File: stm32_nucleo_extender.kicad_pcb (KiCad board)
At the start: 2 copper layers, 103.8 x 162.9 mm, 6 parts, among them CN10 6-534206-9, CN7 6-534206-9, J1 TBL009-254-20GY-2GY, J2 TBL009-254-20GY-2GY, J3 TBL009-254-20GY-2GY, J4 TBL009-254-20GY-2GY

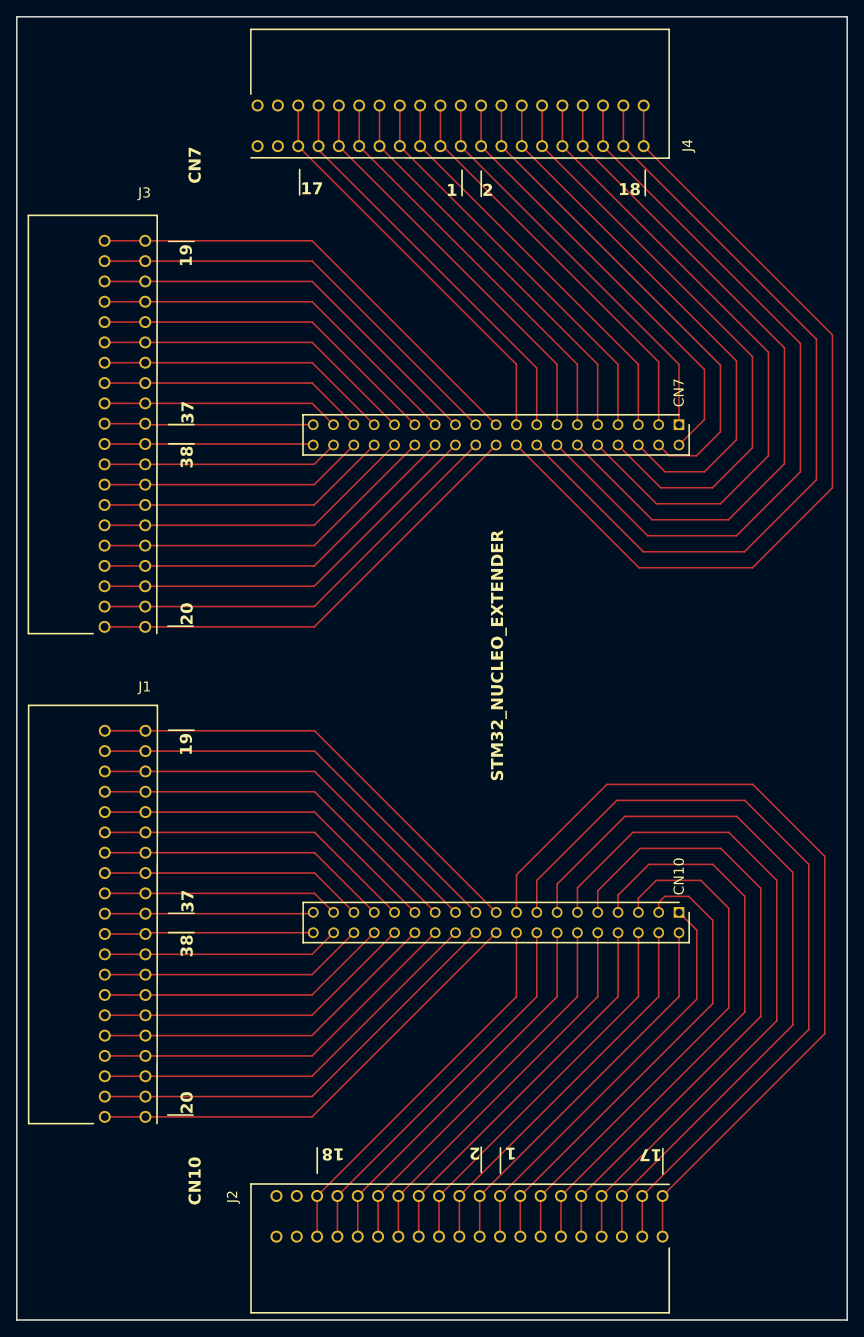
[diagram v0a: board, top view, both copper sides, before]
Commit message: [UPD] to kicad 10.0 [ADD] round tracks
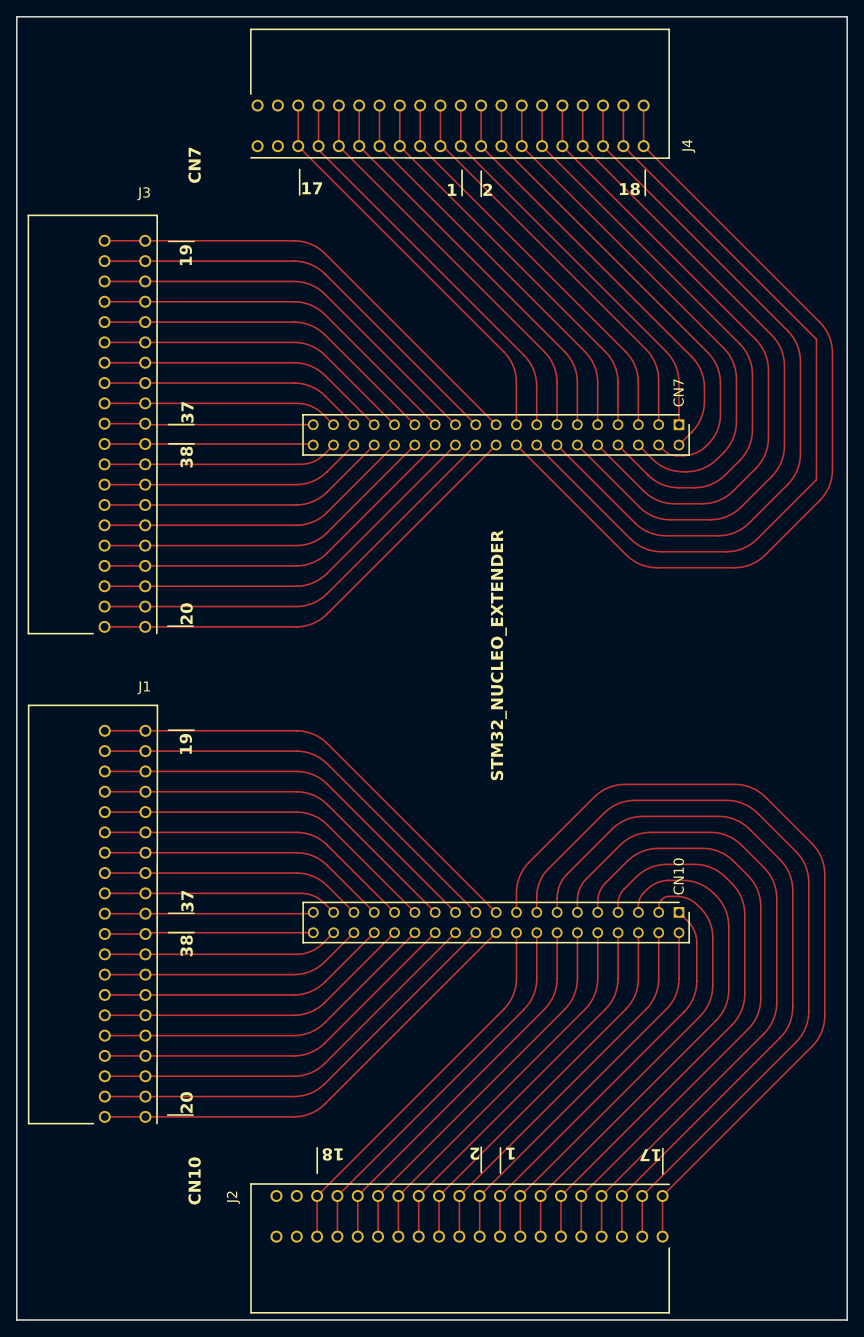
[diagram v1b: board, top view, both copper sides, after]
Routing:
- net /CN10_17: track 107.6 -> 106.3 mm
- net /CN10_15: track 100.6 -> 99.3 mm
- net /CN10_13: track 93.8 -> 92.5 mm
- net /CN10_11: track 87.0 -> 85.7 mm
- net /CN10_9: track 80.2 -> 79.0 mm
- net /CN10_7: track 73.3 -> 72.1 mm
- net /CN10_5: track 66.2 -> 65.1 mm
- net /CN7_8: track 74.9 -> 73.8 mm
- net /CN7_6: track 68.4 -> 67.3 mm
- net /CN7_18: track 107.6 -> 106.5 mm
- net /CN7_14: track 94.7 -> 93.7 mm
- net /CN7_12: track 88.0 -> 87.0 mm
- net /CN7_10: track 81.4 -> 80.4 mm
- net /CN7_4: track 62.1 -> 61.3 mm
- net /CN10_3: track 59.1 -> 58.2 mm
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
